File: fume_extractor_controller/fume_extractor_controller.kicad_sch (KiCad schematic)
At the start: 31 parts, among them J1 Conn_01x02, J2 Conn_01x04, J3 Conn_01x02_Pin, Q1 Q_NMOS_GDS, SW1 SW_SPDT, U1 NE555P, U2 NE555P

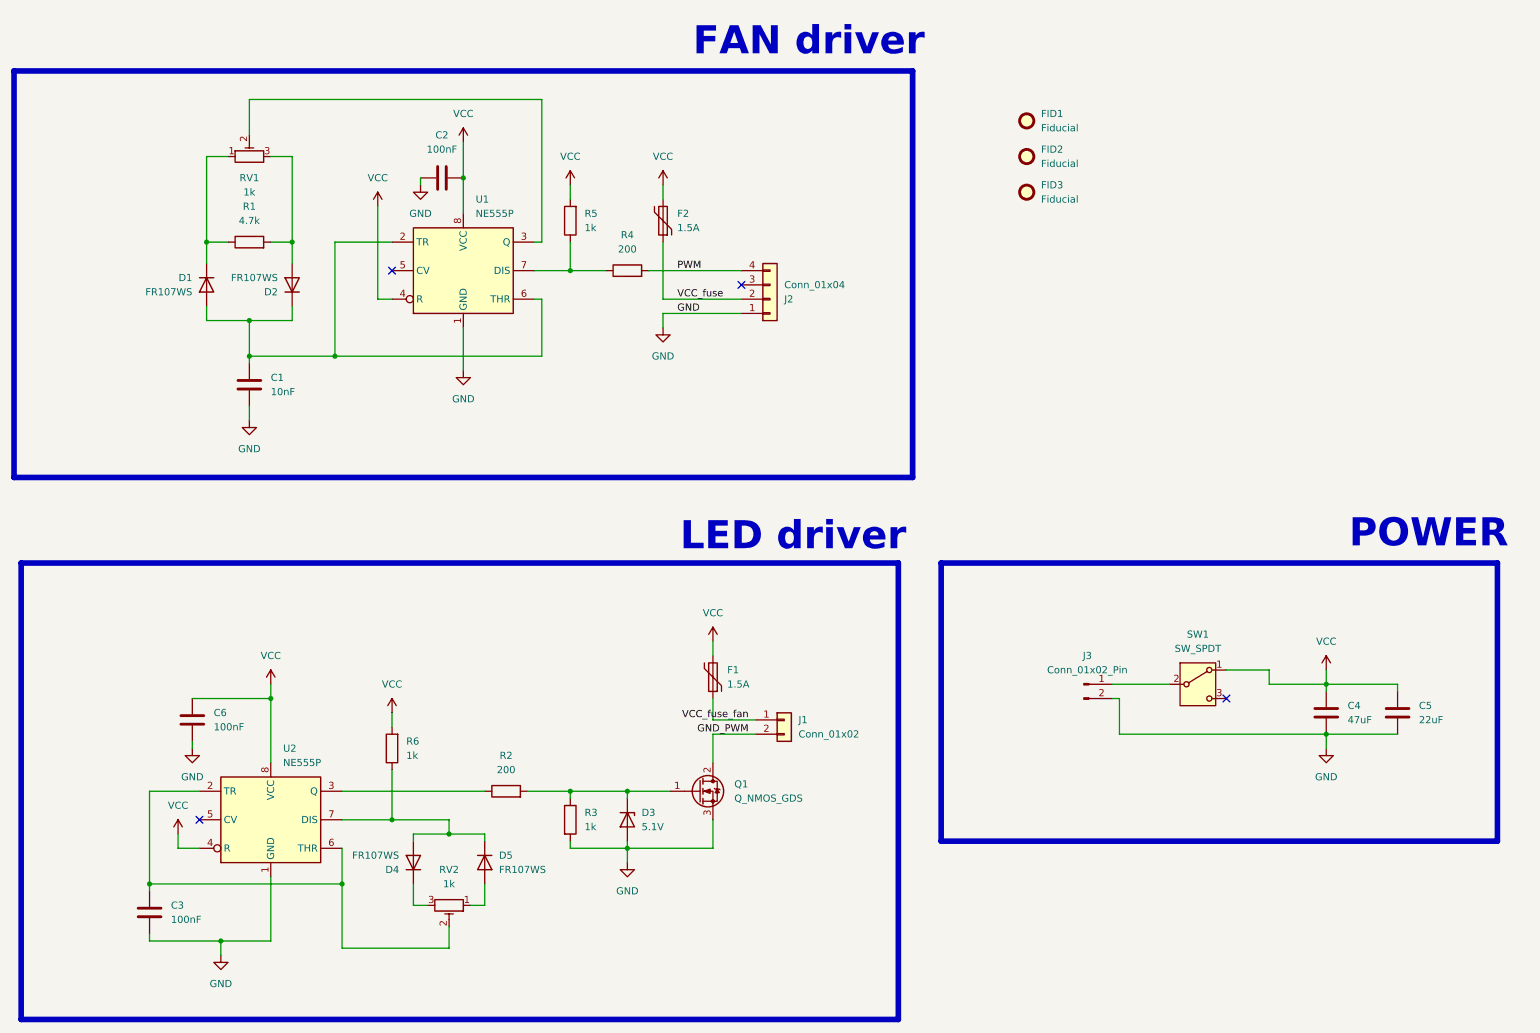
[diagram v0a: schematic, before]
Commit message: Added part numbers and changed mosfet from gds to gsd.
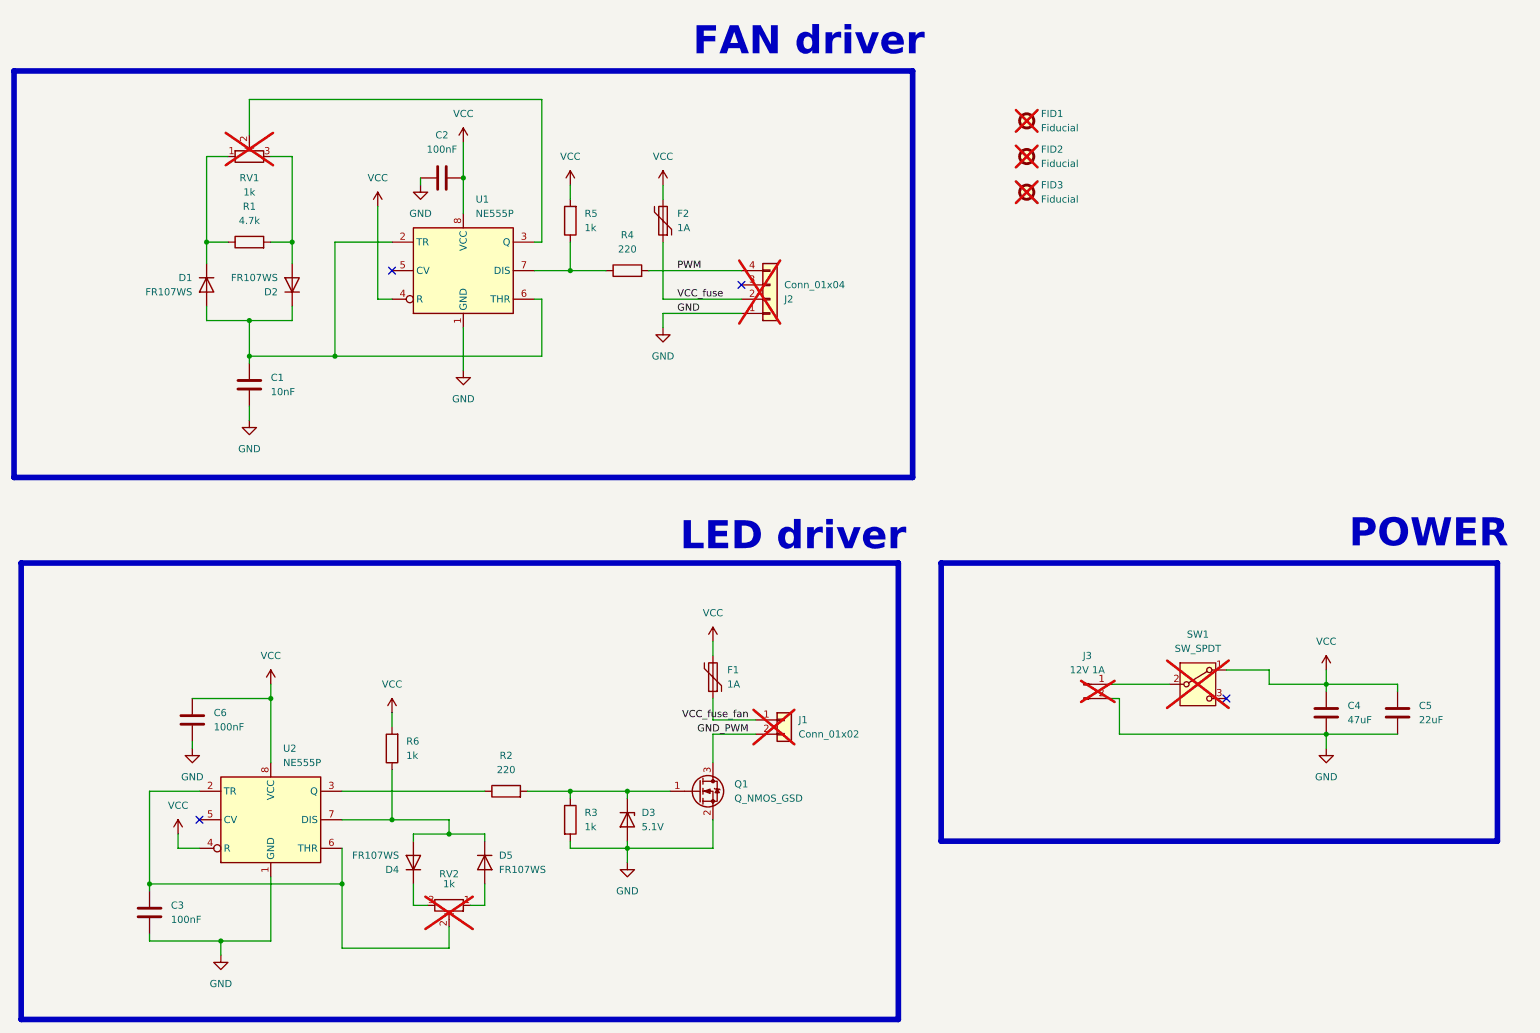
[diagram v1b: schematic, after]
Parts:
- removed Q1: Q_NMOS_GDS, Package_TO_SOT_SMD:SOT-23-3, symbol Device:Q_NMOS_GDS
- added Q1: Q_NMOS_GSD, Package_TO_SOT_SMD:SOT-23, symbol Device:Q_NMOS_GSD
- C1: #LCSC (none) -> C100042
- C2, C3, C6: #LCSC (none) -> C1591
- C4, C5: #LCSC (none) -> C90142
- F1, F2: value 1.5A -> 1A; #LCSC (none) -> C151139
- FID1, FID2, FID3, J1, J2, SW1: now not fitted
- J3: value Conn_01x02_Pin -> 12V 1A; now not fitted
- R1: #LCSC (none) -> C23162
- R2, R4: value 200 -> 220; #LCSC (none) -> C22962
- R3, R5, R6: #LCSC (none) -> C22548
- RV1, RV2: #LCSC (none) -> PT6LH-1K; now not fitted
- U1, U2: #LCSC (none) -> C105643
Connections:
- net GND: now also Q1.2 (S)
- net GND_PWM: now also Q1.3 (D)
- net at D3.1 (K), R2.2, R3.1: now also Q1.1 (G)
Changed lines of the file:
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@@
 		(in_bom yes)
 		(on_board yes)
-		(dnp no)
+		(dnp yes)
 		(property "Reference" "J2"
 			(at 152.4 64.77 0)
@@
 		(in_bom yes)
 		(on_board yes)
-		(dnp no)
-		(fields_autoplaced yes)
+		(dnp yes)
 		(property "Reference" "RV2"
-			(at 92.71 166.37 90)
+			(at 92.71 167.132 90)
 			(effects
 				(font
@@
 			)
 		)
-		(property "Datasheet" "~"
+		(property "Datasheet" "https://www.tme.eu/hu/details/pt6lh-1k/egyfordulatu-tht-trimmerek/piher/pt6kh102a2020/"
 			(at 92.71 172.72 0)
 			(effects
@@
 			)
 		)
-		(property "Description" ""
+		(property "Description" "PT6KH102A2020"
 			(at 92.71 172.72 0)
 			(effects
@@
 			)
 		)
-		(property "#LCSC" ""
+		(property "#LCSC" "PT6LH-1K"
 			(at 92.71 172.72 0)
 			(effects
@@
 			)
 		)
-		(property "#LCSC" ""
+		(property "#LCSC" "C1591"
 			(at 46.99 139.7 0)
 			(effects
@@
 			)
 		)
-		(property "#LCSC" ""
+		(property "#LCSC" "C22548"
 			(at 82.55 144.78 0)
 			(effects
@@
 			)
 		)
-		(property "Value" "1.5A"
+		(property "Value" "1A"
 			(at 133.35 52.07 0)
 			(effects
@@
 			)
 		)
-		(property "#LCSC" ""
+		(property "#LCSC" "C151139"
 			(at 130.81 50.8 0)
 			(effects
@@
 			)
 		)
-		(property "#LCSC" ""
+		(property "#LCSC" "C105643"
 			(at 60.96 157.48 0)
 			(effects
@@
 	)
 	(symbol
-		(lib_id "Device:Q_NMOS_GDS")
-		(at 137.16 152.4 0)
-		(unit 1)
-		(exclude_from_sim no)
-		(in_bom yes)
-		(on_board yes)
-		(dnp no)
-		(fields_autoplaced yes)
-		(property "Reference" "Q1"
-			(at 143.51 151.13 0)
-			(effects
-				(font
-					(size 1.27 1.27)
-				)
-				(justify left)
-			)
-		)
-		(property "Value" "Q_NMOS_GDS"
-			(at 143.51 153.67 0)
-			(effects
-				(font
-					(size 1.27 1.27)
-				)
-				(justify left)
-			)
-		)
-		(property "Footprint" "Package_TO_SOT_SMD:SOT-23-3"
-			(at 142.24 149.86 0)
-			(effects
-				(font
-					(size 1.27 1.27)
-				)
-				(hide yes)
-			)
-		)
-		(property "Datasheet" "~"
-			(at 137.16 152.4 0)
-			(effects
-				(font
-					(size 1.27 1.27)
-				)
-				(hide yes)
-			)
-		)
-		(property "Description" ""
-			(at 137.16 152.4 0)
-			(effects
-				(font
-					(size 1.27 1.27)
-				)
-				(hide yes)
-			)
-		)
-		(property "#LCSC" ""
-			(at 137.16 152.4 0)
-			(effects
-				(font
-					(size 1.27 1.27)
-				)
-				(hide yes)
-			)
-		)
-		(pin "3"
-		)
-		(pin "1"
-		)
-		(pin "2"
-		)
-		(instances
-			(project "fume_extractor_controller"
-				(path "/5c6a8104-81c4-4751-8974-3ee035b73f03"
-					(reference "Q1")
-					(unit 1)
-				)
-			)
-		)
-	)
-	(symbol
 		(lib_id "Device:C")
 		(at 39.37 173.99 180)
@@
 			)
 		)
-		(property "#LCSC" ""
+		(property "#LCSC" "C1591"
 			(at 39.37 173.99 0)
 			(effects
@@
 		(in_bom yes)
 		(on_board yes)
-		(dnp no)
+		(dnp yes)
 		(fields_autoplaced yes)
 		(property "Reference" "FID1"
@@
 		(in_bom yes)
 		(on_board yes)
-		(dnp no)
+		(dnp yes)
 		(fields_autoplaced yes)
 		(property "Reference" "FID2"
@@
 			)
 		)
-		(property "#LCSC" ""
+		(property "#LCSC" "C105643"
 			(at 95.25 59.69 0)
 			(effects
@@
 			)
 		)
-		(property "#LCSC" ""
+		(property "#LCSC" "C90142"
 			(at 261.62 138.43 0)
 			(effects
@@
 			)
 		)
-		(property "Value" "200"
+		(property "Value" "220"
 			(at 124.46 55.88 90)
 			(effects
@@
 			)
 		)
-		(property "#LCSC" ""
+		(property "#LCSC" "C22962"
 			(at 124.46 59.69 0)
 			(effects
@@
 			)
 		)
-		(property "Value" "200"
+		(property "Value" "220"
 			(at 102.87 148.59 90)
 			(effects
@@
 			)
 		)
-		(property "#LCSC" ""
+		(property "#LCSC" "C22962"
 			(at 102.87 152.4 0)
 			(effects
@@
 		(in_bom yes)
 		(on_board yes)
-		(dnp no)
+		(dnp yes)
 		(fields_autoplaced yes)
 		(property "Reference" "J3"
@@
 			)
 		)
-		(property "Value" "Conn_01x02_Pin"
+		(property "Value" "12V 1A"
 			(at 206.375 130.81 0)
 			(effects
@@
 		(in_bom yes)
 		(on_board yes)
-		(dnp no)
+		(dnp yes)
 		(fields_autoplaced yes)
 		(property "Reference" "J1"
@@
 			)
 		)
-		(property "#LCSC" ""
+		(property "#LCSC" "C23162"
 			(at 57.15 54.61 0)
 			(effects
@@
 		(in_bom yes)
 		(on_board yes)
-		(dnp no)
+		(dnp yes)
 		(fields_autoplaced yes)
 		(property "Reference" "SW1"
@@
 	)
 	(symbol
+		(lib_id "Device:Q_NMOS_GSD")
+		(at 137.16 152.4 0)
+		(unit 1)
+		(exclude_from_sim no)
+		(in_bom yes)
+		(on_board yes)
+		(dnp no)
+		(fields_autoplaced yes)
+		(property "Reference" "Q1"
+			(at 143.51 151.1299 0)
+			(effects
+				(font
+					(size 1.27 1.27)
+				)
+				(justify left)
+			)
+		)
+		(property "Value" "Q_NMOS_GSD"
+			(at 143.51 153.6699 0)
+			(effects
+				(font
+					(size 1.27 1.27)
+				)
+				(justify left)
+			)
+		)
+		(property "Footprint" "Package_TO_SOT_SMD:SOT-23"
+			(at 142.24 149.86 0)
+			(effects
+				(font
+					(size 1.27 1.27)
+				)
+				(hide yes)
+			)
+		)
+		(property "Datasheet" "~"
+			(at 137.16 152.4 0)
+			(effects
+				(font
+					(size 1.27 1.27)
+				)
+				(hide yes)
+			)
+		)
+		(property "Description" "N-MOSFET transistor, gate/source/drain"
+			(at 137.16 152.4 0)
+			(effects
+				(font
+					(size 1.27 1.27)
+				)
+				(hide yes)
+			)
+		)
+		(property "#LCSC" "C4748722"
+			(at 137.16 152.4 0)
+			(effects
+				(font
+					(size 1.27 1.27)
+				)
+				(hide yes)
+			)
+		)
+		(pin "3"
+		)
+		(pin "2"
+		)
+		(pin "1"
+		)
+		(instances
+			(project "fume_extractor_controller"
+				(path "/5c6a8104-81c4-4751-8974-3ee035b73f03"
+					(reference "Q1")
+					(unit 1)
+				)
+			)
+		)
+	)
+	(symbol
 		(lib_id "Device:C")
 		(at 91.44 43.18 90)
@@
 			)
 		)
-		(property "#LCSC" ""
+		(property "#LCSC" "C1591"
 			(at 91.44 43.18 0)
 			(effects
@@
 			)
 		)
-		(property "#LCSC" ""
+		(property "#LCSC" "C22548"
 			(at 114.3 50.8 0)
 			(effects
@@
 			)
 		)
-		(property "#LCSC" ""
+		(property "#LCSC" "C100042"
 			(at 57.15 80.01 0)
 			(effects
@@
 			)
 		)
-		(property "Value" "1.5A"
+		(property "Value" "1A"
 			(at 142.24 133.35 0)
 			(effects
@@
 			)
 		)
-		(property "#LCSC" ""
+		(property "#LCSC" "C151139"
 			(at 139.7 132.08 0)
 			(effects
@@
 		(in_bom yes)
 		(on_board yes)
-		(dnp no)
+		(dnp yes)
 		(fields_autoplaced yes)
 		(property "Reference" "FID3"
@@
 			)
 		)
-		(property "#LCSC" ""
+		(property "#LCSC" "C90142"
 			(at 248.92 138.43 0)
 			(effects
@@
 			)
 		)
-		(property "#LCSC" ""
+		(property "#LCSC" "C22548"
 			(at 114.3 157.48 0)
 			(effects
@@
 		(in_bom yes)
 		(on_board yes)
-		(dnp no)
+		(dnp yes)
 		(fields_autoplaced yes)
 		(property "Reference" "RV1"
@@
 			)
 		)
-		(property "Description" ""
+		(property "Description" "PT6KH102A2020"
 			(at 57.15 39.37 0)
 			(effects
@@
 			)
 		)
-		(property "#LCSC" ""
+		(property "#LCSC" "PT6LH-1K"
 			(at 57.15 39.37 0)
 			(effects

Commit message: v1_20052024 added. Production docs generated.
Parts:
- C1: #LCSC C100042 -> (none); MPN (none) -> C100042
- C2, C3, C6: #LCSC C1591 -> (none); MPN (none) -> C1591
- C4: #LCSC C90142 -> (none); MPN (none) -> C90142
- C5: value 22uF -> 47uF; #LCSC C90142 -> (none); MPN (none) -> C90142
- D1, D2, D4, D5: #LCSC C3013756 -> (none); MPN (none) -> C3013756
- D3: #LCSC C2891762 -> (none); MPN (none) -> C2891762
- F1, F2: #LCSC C151139 -> (none); MPN (none) -> C151139
- J2: value Conn_01x04 -> MX-47053-1000; MPN (none) -> MX-47053-1000
- Q1: #LCSC C4748722 -> (none); MPN (none) -> C4748722
- R1: #LCSC C23162 -> (none); MPN (none) -> C23162
- R2, R4: #LCSC C22962 -> (none); MPN (none) -> C22962
- R3, R5, R6: #LCSC C22548 -> (none); MPN (none) -> C22548
- RV1, RV2: #LCSC PT6LH-1K -> (none); MPN (none) -> PT6LH-1K
- SW1: MPN (none) -> OS102011MA1QN1
- U1, U2: #LCSC C105643 -> (none); MPN (none) -> C105643
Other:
- title: (none) -> Fume Extractor Controller
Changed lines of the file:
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@@
 	(generator_version "8.0")
 	(paper "A4")
+	(title_block
+		(title "Fume Extractor Controller")
+		(date "2024-05-20")
+		(rev "1")
+		(comment 1 "Designer: Mark Kovacs")
+	)
 	(junction
 		(at 57.15 74.93)
@@
 			)
 		)
-		(property "Value" "Conn_01x04"
+		(property "Value" "MX-47053-1000"
 			(at 152.4 62.23 0)
 			(effects
@@
 			)
 		)
-		(property "Datasheet" "~"
+		(property "Datasheet" "https://www.tme.eu/hu/details/mx-47053-1000/jelcsatlakozok-raszter-2-54mm/molex/470531000/"
 			(at 149.86 64.77 0)
 			(effects
@@
 			)
 		)
-		(property "#LCSC" ""
+		(property "MPN" "MX-47053-1000"
 			(at 149.86 64.77 0)
 			(effects
@@
 			)
 		)
-		(property "#LCSC" "PT6LH-1K"
+		(property "MPN" "PT6LH-1K"
 			(at 92.71 172.72 0)
 			(effects
@@
 			)
 		)
-		(property "#LCSC" "C1591"
+		(property "MPN" "C1591"
 			(at 46.99 139.7 0)
 			(effects
@@
 			)
 		)
-		(property "#LCSC" "C22548"
+		(property "MPN" "C22548"
 			(at 82.55 144.78 0)
 			(effects
@@
 			)
 		)
-		(property "#LCSC" "C3013756"
+		(property "MPN" "C3013756"
 			(at 49.53 62.23 0)
 			(effects
@@
 			)
 		)
-		(property "#LCSC" "C151139"
+		(property "MPN" "C151139"
 			(at 130.81 50.8 0)
 			(effects
@@
 			)
 		)
-		(property "#LCSC" "C105643"
+		(property "MPN" "C105643"
 			(at 60.96 157.48 0)
 			(effects
@@
 			)
 		)
-		(property "#LCSC" "C1591"
+		(property "MPN" "C1591"
 			(at 39.37 173.99 0)
 			(effects
@@
 			)
 		)
-		(property "#LCSC" "C105643"
+		(property "MPN" "C105643"
 			(at 95.25 59.69 0)
 			(effects
@@
 			)
 		)
-		(property "Value" "22uF"
+		(property "Value" "47uF"
 			(at 265.43 139.6999 0)
 			(effects
@@
 			)
 		)
-		(property "#LCSC" "C90142"
+		(property "MPN" "C90142"
 			(at 261.62 138.43 0)
 			(effects
@@
 			)
 		)
-		(property "#LCSC" "C22962"
+		(property "MPN" "C22962"
 			(at 124.46 59.69 0)
 			(effects
@@
 			)
 		)
-		(property "#LCSC" "C3013756"
+		(property "MPN" "C3013756"
 			(at 99.06 165.1 0)
 			(effects
@@
 			)
 		)
-		(property "#LCSC" "C22962"
+		(property "MPN" "C22962"
 			(at 102.87 152.4 0)
 			(effects
@@
 			)
 		)
-		(property "#LCSC" ""
-			(at 205.74 133.35 0)
-			(effects
-				(font
-					(size 1.27 1.27)
-				)
-				(hide yes)
-			)
-		)
 		(pin "1"
 		)
@@
 			)
 		)
-		(property "#LCSC" ""
-			(at 152.4 139.7 0)
-			(effects
-				(font
-					(size 1.27 1.27)
-				)
-				(hide yes)
-			)
-		)
 		(pin "2"
 		)
@@
 			)
 		)
-		(property "#LCSC" "C23162"
+		(property "MPN" "C23162"
 			(at 57.15 54.61 0)
 			(effects
@@
 			)
 		)
-		(property "Datasheet" "~"
+		(property "Datasheet" "https://www.tme.eu/hu/details/os102011ma1qn1/csuszo-kapcsolok/c-k/"
 			(at 226.06 140.97 0)
 			(effects
@@
 			)
 		)
+		(property "MPN" "OS102011MA1QN1"
+			(at 226.06 133.35 0)
+			(effects
+				(font
+					(size 1.27 1.27)
+				)
+				(hide yes)
+			)
+		)
 		(pin "1"
 		)
@@
 			)
 		)
-		(property "#LCSC" "C2891762"
+		(property "MPN" "C2891762"
 			(at 124.46 157.48 0)
 			(effects
@@
 			)
 		)
-		(property "#LCSC" "C4748722"
+		(property "MPN" "C4748722"
 			(at 137.16 152.4 0)
 			(effects
@@
 			)
 		)
-		(property "#LCSC" "C1591"
+		(property "MPN" "C1591"
 			(at 91.44 43.18 0)
 			(effects
@@
 			)
 		)
-		(property "#LCSC" "C22548"
+		(property "MPN" "C22548"
 			(at 114.3 50.8 0)
 			(effects
@@
 			)
 		)
-		(property "#LCSC" "C3013756"
+		(property "MPN" "C3013756"
 			(at 64.77 62.23 0)
 			(effects
@@
 			)
 		)
-		(property "#LCSC" "C100042"
+		(property "MPN" "C100042"
 			(at 57.15 80.01 0)
 			(effects
@@
 			)
 		)
-		(property "#LCSC" "C3013756"
+		(property "MPN" "C3013756"
 			(at 86.36 165.1 0)
 			(effects
@@
 			)
 		)
-		(property "#LCSC" "C151139"
+		(property "MPN" "C151139"
 			(at 139.7 132.08 0)
 			(effects
@@
 			)
 		)
-		(property "#LCSC" "C90142"
+		(property "MPN" "C90142"
 			(at 248.92 138.43 0)
 			(effects
@@
 			)
 		)
-		(property "#LCSC" "C22548"
+		(property "MPN" "C22548"
 			(at 114.3 157.48 0)
 			(effects
@@
 			)
 		)
-		(property "#LCSC" "PT6LH-1K"
+		(property "MPN" "PT6LH-1K"
 			(at 57.15 39.37 0)
 			(effects

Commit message: verion that i ordered.
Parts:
- C1: MPN C100042 -> C57112
- C2, C3, C6: MPN C1591 -> C14663
- D1, D2, D4, D5: value FR107WS -> 1N4148WS; MPN C3013756 -> C2128
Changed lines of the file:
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@@
 			)
 		)
-		(property "MPN" "C1591"
+		(property "MPN" "C14663"
 			(at 46.99 139.7 0)
 			(effects
@@
 			)
 		)
-		(property "Value" "FR107WS"
+		(property "Value" "1N4148WS"
 			(at 46.99 63.5 90)
 			(effects
@@
 			)
 		)
-		(property "MPN" "C3013756"
+		(property "MPN" "C2128"
 			(at 49.53 62.23 0)
 			(effects
@@
 			)
 		)
-		(property "MPN" "C1591"
+		(property "MPN" "C14663"
 			(at 39.37 173.99 0)
 			(effects
@@
 			)
 		)
-		(property "Value" "FR107WS"
+		(property "Value" "1N4148WS"
 			(at 101.6 166.37 90)
 			(effects
@@
 			)
 		)
-		(property "MPN" "C3013756"
+		(property "MPN" "C2128"
 			(at 99.06 165.1 0)
 			(effects
@@
 			)
 		)
-		(property "MPN" "C1591"
+		(property "MPN" "C14663"
 			(at 91.44 43.18 0)
 			(effects
@@
 			)
 		)
-		(property "Value" "FR107WS"
+		(property "Value" "1N4148WS"
 			(at 62.23 60.96 90)
 			(effects
@@
 			)
 		)
-		(property "MPN" "C3013756"
+		(property "MPN" "C2128"
 			(at 64.77 62.23 0)
 			(effects
@@
 			)
 		)
-		(property "MPN" "C100042"
+		(property "MPN" "C57112"
 			(at 57.15 80.01 0)
 			(effects
@@
 			)
 		)
-		(property "Value" "FR107WS"
+		(property "Value" "1N4148WS"
 			(at 83.82 163.83 90)
 			(effects
@@
 			)
 		)
-		(property "MPN" "C3013756"
+		(property "MPN" "C2128"
 			(at 86.36 165.1 0)
 			(effects

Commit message: final version with html bom and changed component.
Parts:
- D3: MPN C2891762 -> C49585
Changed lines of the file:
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@@
 			)
 		)
-		(property "MPN" "C2891762"
+		(property "MPN" "C49585"
 			(at 124.46 157.48 0)
 			(effects
